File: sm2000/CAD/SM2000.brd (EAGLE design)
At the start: 160 x 100 mm, 407 parts, among them CN1 HDR100-3, CN2 ST-3509, CN3 HDR100-3, CN4 JS-MU3-002, CN5 DS-0518, CN6 ST-3509, CN7 ST-3509, J1 JMP-2PIN, J10 JMPR-2X2, J11 JMPR-2X2, J12 JMPR-2X2, J13 JMPR-2X2, J14 JMPR-2X2, J2 HDR100-7, J3 JMP-2PIN, J4 CONN-BOOM-XH-2A, J5 JMP-2PIN, J6 JMPR-2X2, J7 JMPR-2X2, J8 JMPR-2X2, J9 JMPR-2X2, P1 TPAD50, P10 TPAD50, P2 TPAD50, P3 TPAD50, P4 TPAD50, P5 TPAD50, P6 TPAD50, P7 TPAD50, P8 TPAD50, P9 TPAD50, Q1 MMBT3904, Q10 MMBT3904, Q11 BFR92, Q12 BFQ19, Q13 RD01MUS2, Q14 MMBT3904, Q15 MMBT3904, Q16 MMBT3904, Q17 MMBT3906, Q2 STR2P3LLH6, Q3 MMBT3904, Q4 STR2P3LLH6, Q5 MMBT3904, Q6 MMBT3904, Q7 MMBT3904, Q8 MMBT3904, Q9 MMBT3904, SW1 TS-02B, SW2 SW-LC2259, SW3 TS-026, SW4 TS-026, SW5 SW-LC2259EENP, U1 STM32F405VGT6, U10 LM386M-1, U11 ADE-1, U12 PGA-103+, U13 LMV341, U14 SI5351A, U15 SI570, U16 SA612A, U2 STMPS2141, U3 EMIF02-USB03F2, U4 DNL, U5 L78M09, U6 LD1117AS-33, U7 LMV341, U8 LD1117AS-33, U9 TPS54329E, X1 BU-SMA-H

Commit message: Progress Update. Working on Driver_PA block. RGB
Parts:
- moved L16 317.1 mm to (150.5, -12.5), turned to 90 degrees
- moved L14 296.4 mm to (136.5, -15.0), turned to 180 degrees
- moved J12 295.4 mm to (160.5, -15.0), turned to 90 degrees
- moved L9 258.9 mm to (68.0, -18.0), turned to 180 degrees
- moved C107 251.8 mm to (147.5, -19.5), turned to 270 degrees
- moved L6 246.9 mm to (45.0, -14.0), turned to 270 degrees
- moved C102 245.8 mm to (136.0, -25.0)
- moved C110 244.0 mm to (151.5, -19.5), turned to 270 degrees
- moved C105 241.2 mm to (143.5, -19.5), turned to 270 degrees
- moved Q13 240.0 mm to (125.5, -19.5)
- moved L4 234.7 mm to (18.5, -14.0), turned to 90 degrees
- moved R92 227.7 mm to (119.5, -21.2)
- moved L13 222.0 mm to (124.0, -25.0), turned to 0 degrees
- moved C99 216.4 mm to (119.5, -17.5)
- moved U13 205.4 mm to (89.0, -29.0)
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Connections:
- net GND: now also Q13.4; no longer Q13.2.1
- net N$84: now also Q12.4; no longer Q12.2.1
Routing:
- net N$9: track 0.00 -> 17.1 mm
- net N$52: track 0.00 -> 14.4 mm
- net N$118: track 0.00 -> 13.6 mm
- net N$33: track 0.00 -> 11.3 mm
- net N$32: track 0.00 -> 10.1 mm
- net +9V: track 0.00 -> 6.44 mm
- net N$113: track 0.00 -> 3.72 mm
- net N$130: track 0.00 -> 3.25 mm
- net GND: track 17.9 -> 20.8 mm

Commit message: Progress update and backup. Power supplies laid out. CPU, Mic preamp & Speaker amp next. Looks like adequate room for RF blocks. RGB
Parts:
- removed C83, C88: 2.2pF,50V, _RoweTel:C0805
- removed L7: 260nH, rcl:0204/5
- D4: value BAT60J -> B330B; device _RoweTel:SOD323R_INFINEON -> _RoweTel:SMB
- LED7: value SML-LX0603GW -> LTST-S220KGKT; device _RoweTel:SML-LX0603SRW -> _RoweTel:LTST-S2200K
- XTAL3, XTAL4: device _RoweTel:HC49/S -> _RoweTel:HC49U
- moved D9 359.6 mm to (296.5, 22.0)
- moved R90 355.7 mm to (305.0, 18.5)
- moved R95 353.2 mm to (305.0, 22.0), turned to 0 degrees
- moved C95 351.7 mm to (285.5, 32.0), turned to 0 degrees
- moved C92 347.6 mm to (285.5, 25.0), turned to 0 degrees
- moved D8 332.1 mm to (285.0, 28.0)
- moved L11 329.3 mm to (313.0, 24.0)
- moved C103 328.9 mm to (300.5, 18.5)
- moved C96 324.7 mm to (300.5, 22.0)
- moved C77 321.3 mm to (258.0, 31.0)
- moved L10 321.2 mm to (294.0, 25.5)
- moved U12 321.1 mm to (263.5, 30.0)
- moved L5 321.1 mm to (269.5, 15.0)
- moved L8 321.1 mm to (280.5, 15.0)
- moved R94 320.7 mm to (302.0, 32.0)
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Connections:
- removed net N$139: C83.1, C88.2, L7.1
- removed net N$30: C88.1
- removed net N$36: C83.2
- net GND: now also XTAL3.2, XTAL4.2; no longer L7.2
- net N$143: now also XTAL3.3; no longer XTAL3.1
- net N$144: now also XTAL3.1, XTAL4.1; no longer XTAL3.2, XTAL4.2
- net N$145: now also XTAL4.3; no longer XTAL4.1
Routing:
- net N$81: track 0.00 -> 148.1 mm, vias 0 -> 3
- net +VIN: track 6.28 -> 149.7 mm, vias 1 -> 9
- net GND: track 20.8 -> 68.0 mm, vias 19 -> 33
- net SW: track 2.38 -> 26.4 mm, vias 8 -> 9
- net N$77: track 16.9 -> 39.7 mm
- net N$150: track 0.00 -> 20.3 mm
- net N$129: track 17.9 -> 0.00 mm, vias 0 -> 1
- net +5V: track 0.00 -> 17.8 mm, vias 0 -> 6
- net N$9: track 17.1 -> 0.00 mm
- net N$172: track 0.00 -> 16.1 mm
- net N$110: track 0.00 -> 14.7 mm
- net N$52: track 14.4 -> 0.00 mm
- net N$118: track 13.6 -> 0.00 mm
- net N$33: track 11.3 -> 0.00 mm
- net N$173: track 0.00 -> 10.7 mm
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- added copper zone on layer 1, net 3V3
- added copper zone on layer 3, net 3V3
- added copper zone on layer 1, net A3V3
- added copper zone on layer 3, net A3V3
- added copper zone on layer 16, net GND
- added copper zone on layer 1, net N$170
- added copper zone on layer 3, net SW
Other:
- board text added: "+5V"
- board text added: "1st_MIXER_BPF_SWITCH"
- board text added: "CPU"
- board text added: "DRIVER_PA"

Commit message: Latest schematic, PCB and associated files. Represents work through 03/11/2016  RGB
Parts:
- removed C116: 2-12pF, c-trimm:3008
- removed P1, P10, P2, P3, P4, P5: TPAD50, _Coherix:TPAD50
- added C83: 2-12pF, _RoweTel:TRIMCAP_VAR_2222_V
- C104, C108, C125, C84, C90, C94: value 0.1uF.25V -> 100nF,25V
- C111, C113, C114, C117, C118, C119, C120, C121, C127, C133, C134: value 0.1uF,25V -> 100nF,25V
- C16: value 1uF,16V -> 1uF,25V
- C54: value 22uF,25V,1210 -> 22uF,25V; device AA-ipc-7351-capacitor:CAPC3225X168N -> _RoweTel:C1210
- C64: value 12pF.50V -> 12pF,50V
- L20: value 15uH -> 15uH,TDK,MLF
- R34, R40, R44: value 320,1% -> 330,1%
- XTAL1: value XTAL-FY0800035 -> 8.000MHz; device _RoweTel:XTAL-FY0800035 -> _RoweTel:CTS-405
- XTAL2: value 25MHz,TXC,SMD -> 25.000MHz; device _RoweTel:XTAL-FY0800035 -> _RoweTel:CTS-405
- moved XTAL2 139.3 mm to (42.0, 94.0), turned to 0 degrees
- moved U14 138.8 mm to (42.5, 88.0)
- moved R100 137.6 mm to (52.5, 87.0)
- moved FB15 137.5 mm to (35.5, 92.5)
- moved C111 137.3 mm to (35.5, 79.0), turned to 180 degrees
- moved C113 137.3 mm to (35.5, 85.0), turned to 180 degrees
- moved FB13 137.3 mm to (35.5, 82.0)
- moved FB14 137.3 mm to (35.5, 88.0)
- moved R101 137.3 mm to (52.5, 94.5)
- moved R96 137.3 mm to (52.5, 84.5)
- moved R97 137.3 mm to (52.5, 82.0)
- moved R98 137.3 mm to (52.5, 79.5)
- moved R99 137.3 mm to (52.5, 92.0)
- moved U15 137.3 mm to (43.5, 81.5)
- moved R102 137.1 mm to (52.5, 89.5)
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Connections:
- net N$12 renamed VDDA
- net N$2 renamed VBAT
- net N$5 renamed VREF+
- new net N$2: U14.2
- net +12VRXENB: now also R46.1; no longer R54.1
- net +12VTXENB: now also R54.1; no longer R46.1
- net +5V: no longer P5.1
- net +VIN: no longer P10.1
- net 3V3: no longer P1.1
- net GND: now also C83.S; no longer C116.-, P2.1, P3.1, P4.1, XTAL1.2
- net N$145: now also C83.R1, C83.R2; no longer C116.+
- net N$65: now also XTAL2.1; no longer U14.2, XTAL2.3
- net N$80: now also XTAL2.3; no longer XTAL2.1
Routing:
- net !EXT-PTT!: track 0.00 -> 120.1 mm
- net GND: track 68.0 -> 172.1 mm, vias 33 -> 49
- net N$14: track 8.81 -> 107.6 mm
- net LED-ERR: track 0.00 -> 90.4 mm
- net LED-RT: track 0.00 -> 86.5 mm
- net LED-PTT: track 0.00 -> 82.5 mm
- net LED-PWR: track 0.00 -> 78.7 mm
- net !SELECT!: track 0.00 -> 75.3 mm
- net !BACK!: track 0.00 -> 68.5 mm
- net N$76: track 0.00 -> 41.0 mm
- net 3V3: track 0.00 -> 30.0 mm, vias 8 -> 13
- net N$64: track 0.00 -> 24.4 mm
- net N$27: track 0.00 -> 21.3 mm
- net N$62: track 0.00 -> 20.3 mm
- net N$15: track 0.00 -> 18.8 mm
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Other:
- board text added: "BACK"
- board text added: "CLIP/ ERROR"
- board text added: "EXT MIC"
- board text added: "EXT PTT"
- board text added: "MIC"
- board text added: "POWER"
- board text added: "PTT"
- board text added: "SELECT"
- board text added: "SYNC"

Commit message: Updating to current status. Moved parts onto brd and made BOM current. RGB
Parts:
- moved C135 192.4 mm to (75.0, 66.5), turned to 180 degrees
- moved C123 192.3 mm to (75.0, 78.0), turned to 0 degrees
- moved L20 192.1 mm to (75.0, 69.0), turned to 270 degrees
- moved L19 192.1 mm to (75.0, 75.0), turned to 270 degrees
- moved C132 192.0 mm to (75.0, 72.0), turned to 0 degrees
- moved C124 184.3 mm to (79.0, 78.0), turned to 0 degrees
- moved C125 183.4 mm to (79.5, 66.5), turned to 0 degrees
- moved U16 177.0 mm to (82.5, 71.0), turned to 270 degrees
- moved C128 175.4 mm to (83.5, 66.5), turned to 0 degrees
- moved C133 170.4 mm to (86.0, 78.5), turned to 0 degrees
- moved C131 170.1 mm to (86.0, 75.5), turned to 0 degrees
- moved C102 168.9 mm to (124.5, 11.0)
- moved C104 168.9 mm to (108.5, 17.5)
- moved C105 168.9 mm to (132.5, 10.0)
- moved C106 168.9 mm to (112.0, 17.5)
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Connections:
- removed net N$65: XTAL2.1
- net GND: now also XTAL1.2
- net N$2: now also XTAL2.1
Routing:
- net N$2: track 1.77 -> 0.00 mm

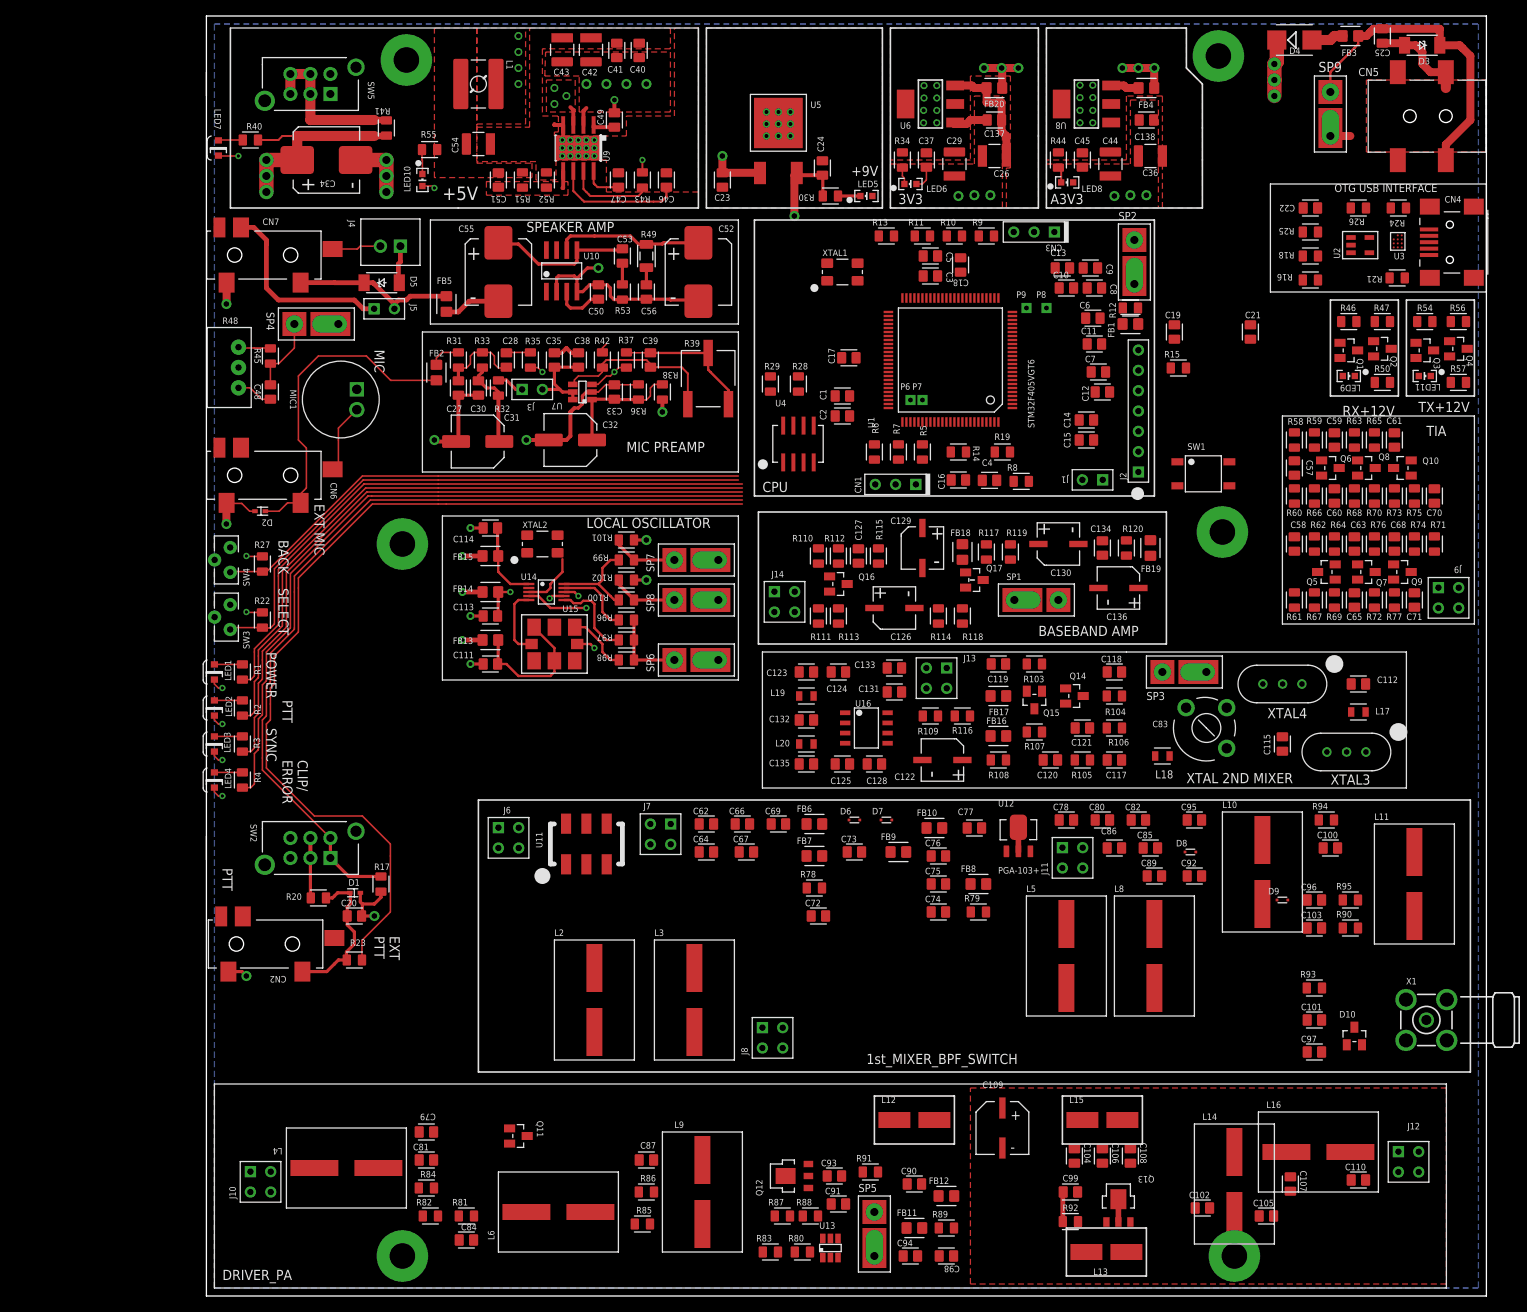
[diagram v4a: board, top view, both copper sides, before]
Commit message: Added Shield mounting tabs(7) to schematic & PCB. Moved, rotated and restructured RF blocks on PCB in proparation for routing. RGB
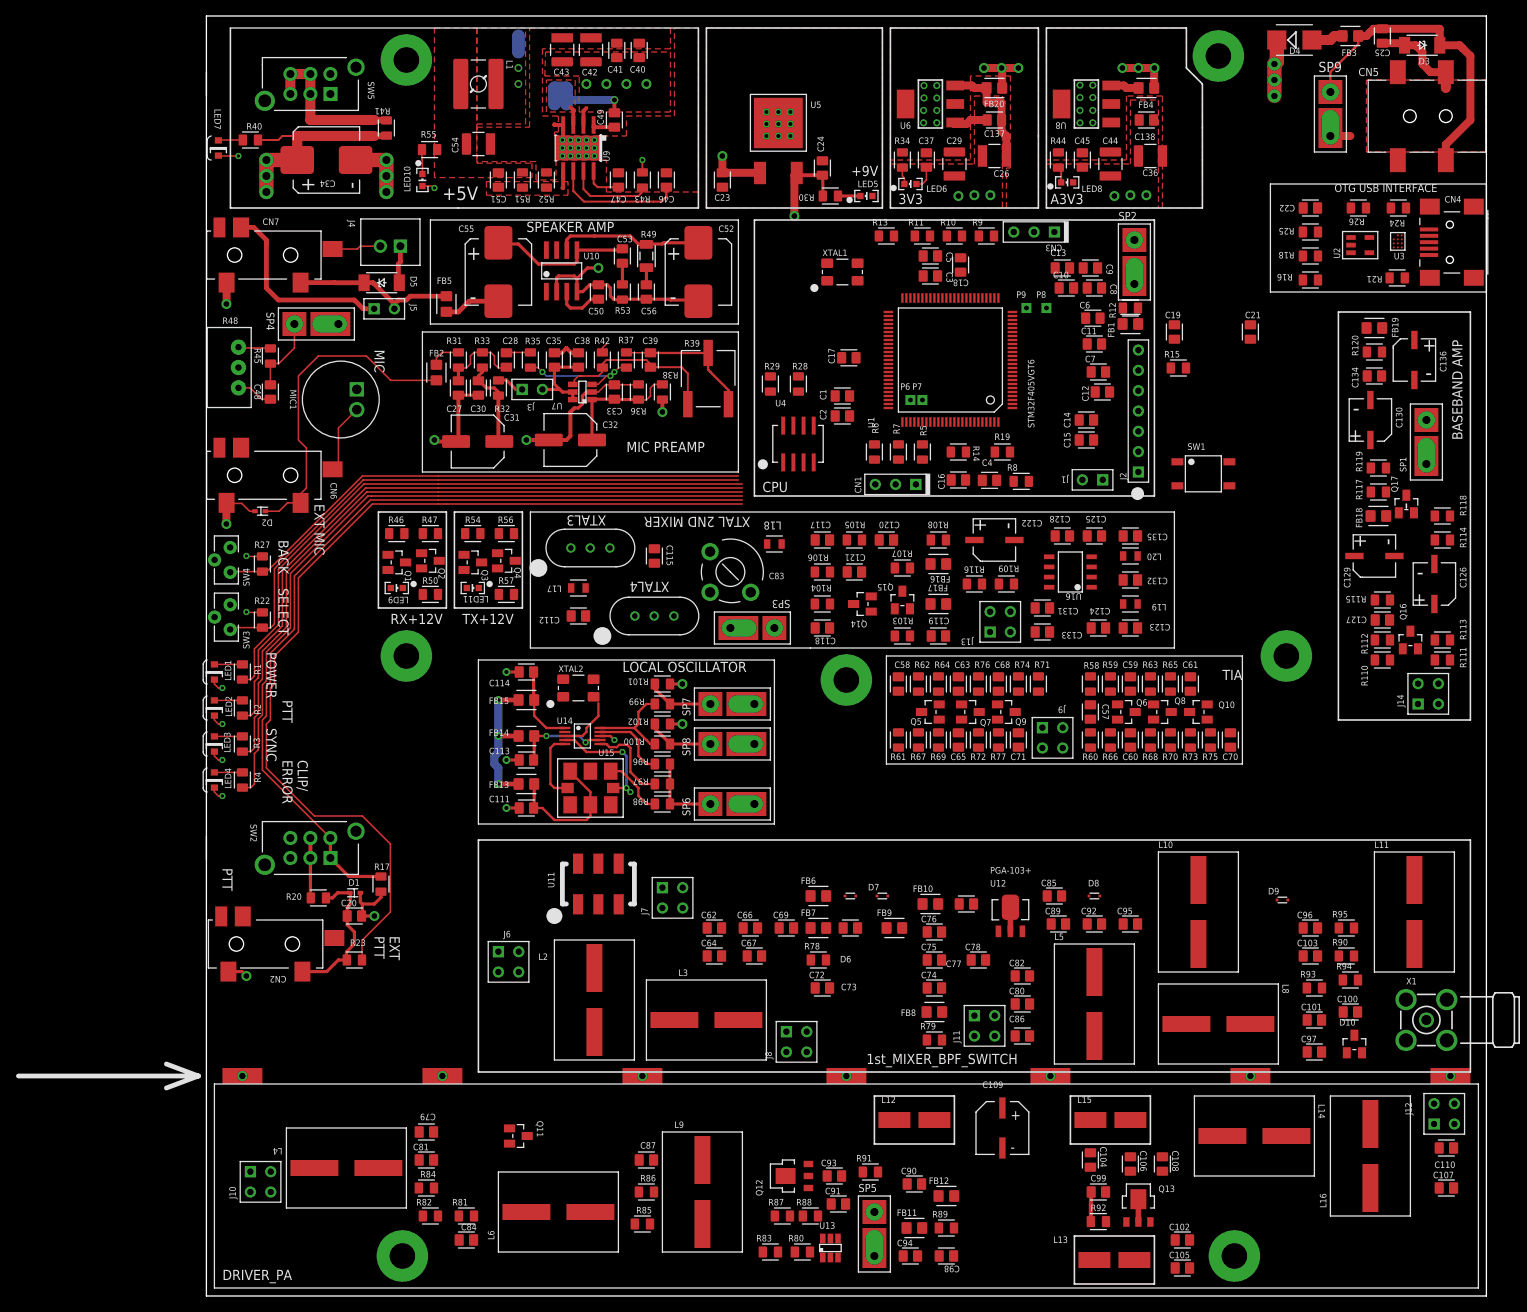
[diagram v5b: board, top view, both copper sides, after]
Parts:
- added S1, S2, S3, S4, S5, S6, S7: SGND, _RoweTel:SGND
- moved LED11 121.9 mm to (33.3, 88.5)
- moved LED9 121.9 mm to (23.8, 88.5)
- moved Q1 121.9 mm to (23.8, 91.7)
- moved Q3 121.9 mm to (33.3, 91.7)
- moved R46 121.9 mm to (23.8, 95.3)
- moved R54 121.9 mm to (33.3, 95.3)
- moved Q2 121.9 mm to (28.0, 91.9)
- moved Q4 121.9 mm to (37.5, 91.9)
- moved R47 121.9 mm to (28.0, 95.3)
- moved R50 121.9 mm to (28.0, 87.7)
- moved R56 121.9 mm to (37.5, 95.3)
- moved R57 121.9 mm to (37.5, 87.7)
- moved L17 98.7 mm to (46.5, 88.5), turned to 90 degrees
- moved XTAL3 97.9 mm to (48.0, 93.5), turned to 0 degrees
- moved C112 97.9 mm to (46.5, 85.0), turned to 180 degrees
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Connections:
- net GND: now also S1.SGND, S2.SGND, S3.SGND, S4.SGND, S5.SGND, S6.SGND, S7.SGND
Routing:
- net GND: track 172.1 -> 173.1 mm, vias 49 -> 50
- net SW: vias 8 -> 3
- net SCL3: vias 2 -> 3
- net N$87: vias 2 -> 3
- added copper zone on layer 2, net GND
- removed copper zone on layer 16, net GND
